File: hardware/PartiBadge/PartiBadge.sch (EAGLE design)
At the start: 18 parts, among them IC1 SI7021-A10-IM, J2 TFT Display Connector

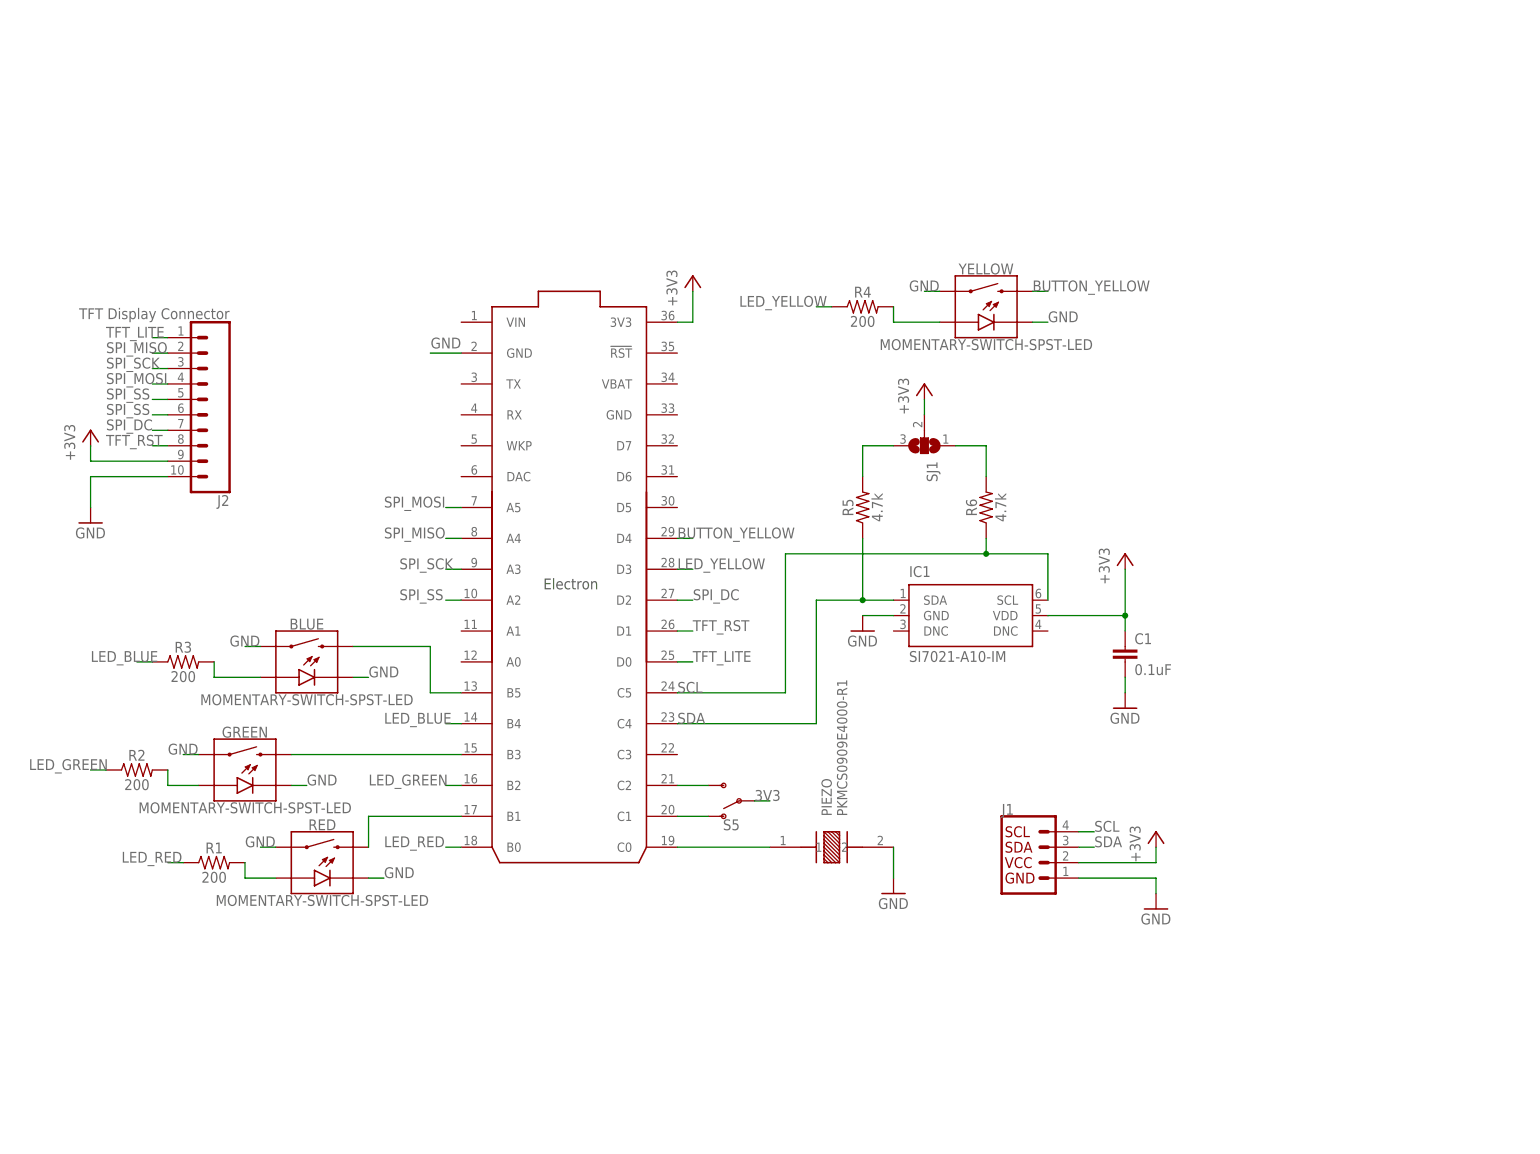
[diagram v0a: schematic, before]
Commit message: tweak layout for smaller badge
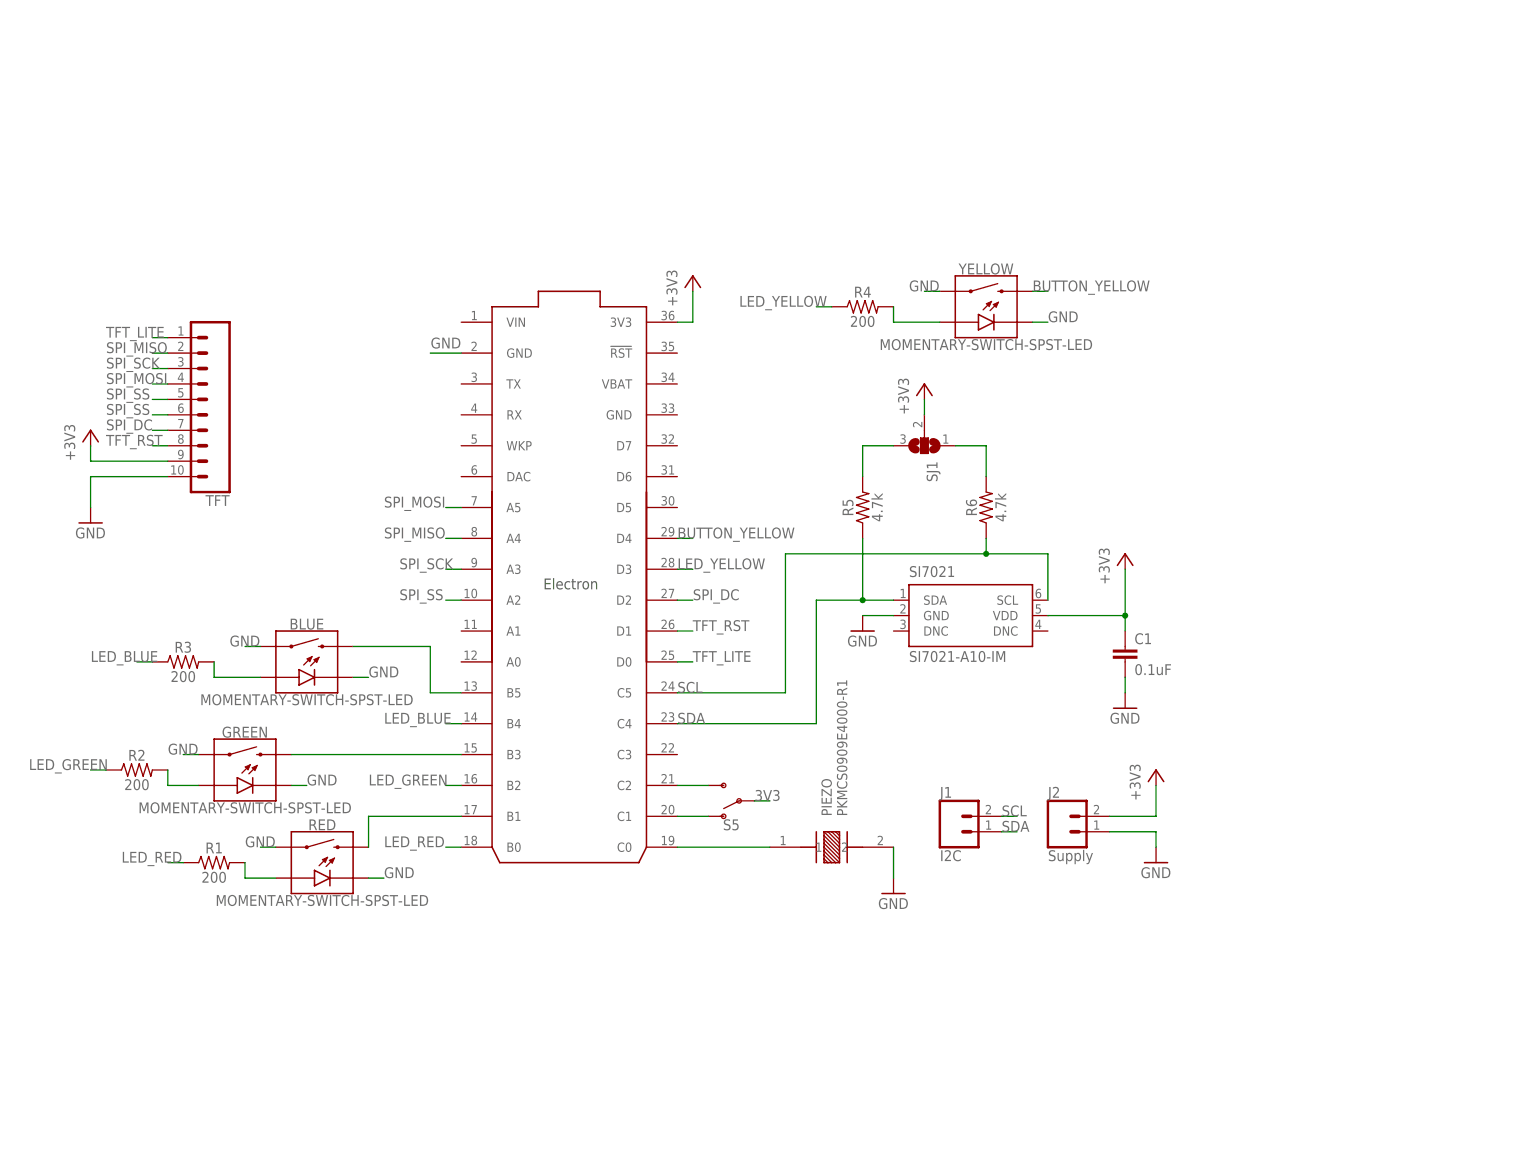
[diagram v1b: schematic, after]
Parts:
- added TFT: (no value), SparkFun-Connectors:CONN_10NO_SILK_PTH_FEMALE
- J1: value (none) -> I2C; device SparkFun-Connectors:I2C_STANDARD -> SparkFun-Connectors:CONN_02
- J2: value TFT Display Connector -> Supply; device SparkFun-Connectors:CONN_10NO_SILK_PTH_FEMALE -> SparkFun-Connectors:CONN_02; SPICEPREFIX X -> (none)
- renumbered IC1 to SI7021, U$1 to ELECTRON
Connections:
- net 3V3: now also J2.2, TFT.9; no longer J1.2, J2.9
- net GND: now also J2.1, TFT.10; no longer J1.1, J2.10
- net SCL: now also J1.2; no longer J1.4
- net SDA: now also J1.1; no longer J1.3
- net SPI_DC: now also TFT.7; no longer J2.7
- net SPI_MISO: now also TFT.2; no longer J2.2
- net SPI_MOSI: now also TFT.4; no longer J2.4
- net SPI_SCK: now also TFT.3; no longer J2.3
- net SPI_SS: now also TFT.5, TFT.6; no longer J2.5, J2.6
- net TFT_LITE: now also TFT.1; no longer J2.1
- net TFT_RST: now also TFT.8; no longer J2.8

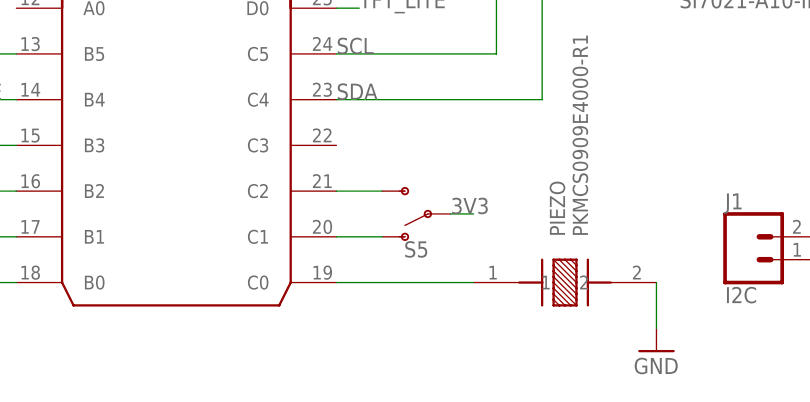
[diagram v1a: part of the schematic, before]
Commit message: increase text and add clr on piezo
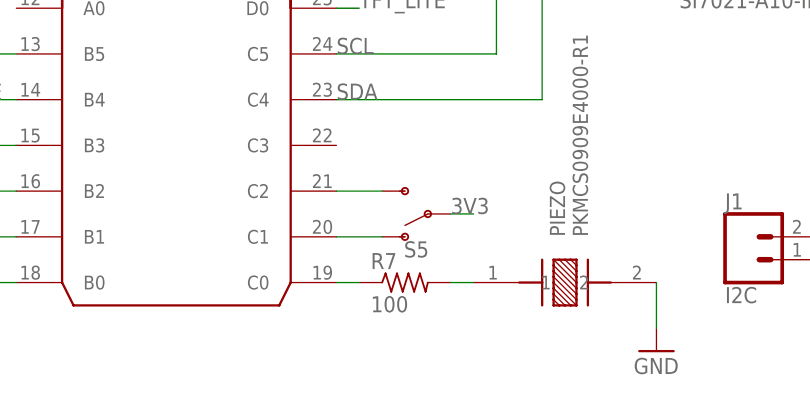
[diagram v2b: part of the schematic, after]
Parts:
- added R7: 100, rcl:R-US_M0805
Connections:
- new net N$13: PIEZO.1, R7.2
- net N$1: now also R7.1; no longer PIEZO.1
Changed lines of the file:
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@@
 <grid distance="0.1" unitdist="inch" unit="inch" style="lines" multiple="1" display="no" altdistance="0.01" altunitdist="inch" altunit="inch"/>
 <layers>
-<layer number="1" name="Top" color="4" fill="1" visible="no" active="no"/>
-<layer number="2" name="Route2" color="1" fill="3" visible="no" active="no"/>
-<layer number="3" name="Route3" color="4" fill="3" visible="no" active="no"/>
-<layer number="4" name="Route4" color="1" fill="4" visible="no" active="no"/>
-<layer number="5" name="Route5" color="4" fill="4" visible="no" active="no"/>
-<layer number="6" name="Route6" color="1" fill="8" visible="no" active="no"/>
-<layer number="7" name="Route7" color="4" fill="8" visible="no" active="no"/>
-<layer number="8" name="Route8" color="1" fill="2" visible="no" active="no"/>
-<layer number="9" name="Route9" color="4" fill="2" visible="no" active="no"/>
-<layer number="10" name="Route10" color="1" fill="7" visible="no" active="no"/>
-<layer number="11" name="Route11" color="4" fill="7" visible="no" active="no"/>
-<layer number="12" name="Route12" color="1" fill="5" visible="no" active="no"/>
-<layer number="13" name="Route13" color="4" fill="5" visible="no" active="no"/>
-<layer number="14" name="Route14" color="1" fill="6" visible="no" active="no"/>
-<layer number="15" name="Route15" color="4" fill="6" visible="no" active="no"/>
-<layer number="16" name="Bottom" color="1" fill="1" visible="no" active="no"/>
-<layer number="17" name="Pads" color="2" fill="1" visible="no" active="no"/>
-<layer number="18" name="Vias" color="2" fill="1" visible="no" active="no"/>
-<layer number="19" name="Unrouted" color="6" fill="1" visible="no" active="no"/>
-<layer number="20" name="Dimension" color="15" fill="1" visible="no" active="no"/>
-<layer number="21" name="tPlace" color="7" fill="1" visible="no" active="no"/>
-<layer number="22" name="bPlace" color="7" fill="1" visible="no" active="no"/>
-<layer number="23" name="tOrigins" color="15" fill="1" visible="no" active="no"/>
-<layer number="24" name="bOrigins" color="15" fill="1" visible="no" active="no"/>
-<layer number="25" name="tNames" color="7" fill="1" visible="no" active="no"/>
-<layer number="26" name="bNames" color="7" fill="1" visible="no" active="no"/>
-<layer number="27" name="tValues" color="7" fill="1" visible="no" active="no"/>
-<layer number="28" name="bValues" color="7" fill="1" visible="no" active="no"/>
+<layer number="1" name="Top" color="4" fill="1" visible="yes" active="no"/>
+<layer number="2" name="Route2" color="1" fill="3" visible="yes" active="no"/>
+<layer number="3" name="Route3" color="4" fill="3" visible="yes" active="no"/>
+<layer number="4" name="Route4" color="1" fill="4" visible="yes" active="no"/>
+<layer number="5" name="Route5" color="4" fill="4" visible="yes" active="no"/>
+<layer number="6" name="Route6" color="1" fill="8" visible="yes" active="no"/>
+<layer number="7" name="Route7" color="4" fill="8" visible="yes" active="no"/>
+<layer number="8" name="Route8" color="1" fill="2" visible="yes" active="no"/>
+<layer number="9" name="Route9" color="4" fill="2" visible="yes" active="no"/>
+<layer number="10" name="Route10" color="1" fill="7" visible="yes" active="no"/>
+<layer number="11" name="Route11" color="4" fill="7" visible="yes" active="no"/>
+<layer number="12" name="Route12" color="1" fill="5" visible="yes" active="no"/>
+<layer number="13" name="Route13" color="4" fill="5" visible="yes" active="no"/>
+<layer number="14" name="Route14" color="1" fill="6" visible="yes" active="no"/>
+<layer number="15" name="Route15" color="4" fill="6" visible="yes" active="no"/>
+<layer number="16" name="Bottom" color="1" fill="1" visible="yes" active="no"/>
+<layer number="17" name="Pads" color="2" fill="1" visible="yes" active="no"/>
+<layer number="18" name="Vias" color="2" fill="1" visible="yes" active="no"/>
+<layer number="19" name="Unrouted" color="6" fill="1" visible="yes" active="no"/>
+<layer number="20" name="Dimension" color="24" fill="1" visible="yes" active="no"/>
+<layer number="21" name="tPlace" color="7" fill="1" visible="yes" active="no"/>
+<layer number="22" name="bPlace" color="7" fill="1" visible="yes" active="no"/>
+<layer number="23" name="tOrigins" color="15" fill="1" visible="yes" active="no"/>
+<layer number="24" name="bOrigins" color="15" fill="1" visible="yes" active="no"/>
+<layer number="25" name="tNames" color="7" fill="1" visible="yes" active="no"/>
+<layer number="26" name="bNames" color="7" fill="1" visible="yes" active="no"/>
+<layer number="27" name="tValues" color="7" fill="1" visible="yes" active="no"/>
+<layer number="28" name="bValues" color="7" fill="1" visible="yes" active="no"/>
 <layer number="29" name="tStop" color="7" fill="3" visible="no" active="no"/>
 <layer number="30" name="bStop" color="7" fill="6" visible="no" active="no"/>
@@
 <layer number="35" name="tGlue" color="7" fill="4" visible="no" active="no"/>
 <layer number="36" name="bGlue" color="7" fill="5" visible="no" active="no"/>
-<layer number="37" name="tTest" color="7" fill="1" visible="no" active="no"/>
-<layer number="38" name="bTest" color="7" fill="1" visible="no" active="no"/>
+<layer number="37" name="tTest" color="7" fill="1" visible="yes" active="no"/>
+<layer number="38" name="bTest" color="7" fill="1" visible="yes" active="no"/>
 <layer number="39" name="tKeepout" color="4" fill="11" visible="no" active="no"/>
 <layer number="40" name="bKeepout" color="1" fill="11" visible="no" active="no"/>
@@
 <layer number="44" name="Drills" color="7" fill="1" visible="no" active="no"/>
 <layer number="45" name="Holes" color="7" fill="1" visible="no" active="no"/>
-<layer number="46" name="Milling" color="3" fill="1" visible="no" active="no"/>
-<layer number="47" name="Measures" color="7" fill="1" visible="no" active="no"/>
-<layer number="48" name="Document" color="7" fill="1" visible="no" active="no"/>
-<layer number="49" name="Reference" color="7" fill="1" visible="no" active="no"/>
-<layer number="50" name="dxf" color="7" fill="1" visible="no" active="no"/>
-<layer number="51" name="tDocu" color="7" fill="1" visible="no" active="no"/>
-<layer number="52" name="bDocu" color="7" fill="1" visible="no" active="no"/>
-<layer number="53" name="tGND_GNDA" color="7" fill="9" visible="no" active="no"/>
-<layer number="54" name="bGND_GNDA" color="1" fill="9" visible="no" active="no"/>
-<layer number="56" name="wert" color="7" fill="1" visible="no" active="no"/>
-<layer number="57" name="tCAD" color="7" fill="1" visible="no" active="no"/>
-<layer number="59" name="tCarbon" color="7" fill="1" visible="no" active="no"/>
-<layer number="60" name="bCarbon" color="7" fill="1" visible="no" active="no"/>
+<layer number="46" name="Milling" color="3" fill="1" visible="yes" active="no"/>
+<layer number="47" name="Measures" color="7" fill="1" visible="yes" active="no"/>
+<layer number="48" name="Document" color="7" fill="1" visible="yes" active="no"/>
+<layer number="49" name="Reference" color="7" fill="1" visible="yes" active="no"/>
+<layer number="50" name="dxf" color="7" fill="1" visible="yes" active="no"/>
+<layer number="51" name="tDocu" color="7" fill="1" visible="yes" active="no"/>
+<layer number="52" name="bDocu" color="7" fill="1" visible="yes" active="no"/>
+<layer number="53" name="tGND_GNDA" color="7" fill="9" visible="yes" active="no"/>
+<layer number="54" name="bGND_GNDA" color="1" fill="9" visible="yes" active="no"/>
+<layer number="56" name="wert" color="7" fill="1" visible="yes" active="no"/>
+<layer number="57" name="tCAD" color="7" fill="1" visible="yes" active="no"/>
+<layer number="59" name="tCarbon" color="7" fill="1" visible="yes" active="no"/>
+<layer number="60" name="bCarbon" color="7" fill="1" visible="yes" active="no"/>
 <layer number="88" name="SimResults" color="9" fill="1" visible="yes" active="yes"/>
 <layer number="89" name="SimProbes" color="9" fill="1" visible="yes" active="yes"/>
@@
 <part name="J1" library="SparkFun-Connectors" library_urn="urn:adsk.eagle:library:513" deviceset="CONN_02" device="" package3d_urn="urn:adsk.eagle:package:38039/1" value="I2C"/>
 <part name="J2" library="SparkFun-Connectors" library_urn="urn:adsk.eagle:library:513" deviceset="CONN_02" device="" package3d_urn="urn:adsk.eagle:package:38039/1" value="Supply"/>
+<part name="R7" library="rcl" library_urn="urn:adsk.eagle:library:334" deviceset="R-US_" device="M0805" package3d_urn="urn:adsk.eagle:package:23556/1" value="100"/>
 </parts>
 <sheets>
@@
 <instance part="J1" gate="G$1" x="93.98" y="10.16"/>
 <instance part="J2" gate="G$1" x="111.76" y="10.16"/>
+<instance part="R7" gate="G$1" x="55.88" y="7.62"/>
 </instances>
 <busses>
 </busses>
 <nets>
-<net name="N$1" class="0">
-<segment>
-<pinref part="ELECTRON" gate="G$1" pin="C0"/>
-<pinref part="PIEZO" gate="G$1" pin="1"/>
-<wire x1="48.26" y1="7.62" x2="63.5" y2="7.62" width="0.1524" layer="91"/>
-</segment>
-</net>
 <net name="GND" class="0">
 <segment>
@@
 <wire x1="-35.56" y1="76.2" x2="-38.1" y2="76.2" width="0.1524" layer="91"/>
 <label x="-45.72" y="76.2" size="1.778" layer="95"/>
+</segment>
+</net>
+<net name="N$1" class="0">
+<segment>
+<pinref part="ELECTRON" gate="G$1" pin="C0"/>
+<pinref part="R7" gate="G$1" pin="1"/>
+<wire x1="48.26" y1="7.62" x2="50.8" y2="7.62" width="0.1524" layer="91"/>
+</segment>
+</net>
+<net name="N$13" class="0">
+<segment>
+<pinref part="R7" gate="G$1" pin="2"/>
+<pinref part="PIEZO" gate="G$1" pin="1"/>
+<wire x1="60.96" y1="7.62" x2="63.5" y2="7.62" width="0.1524" layer="91"/>
 </segment>
 </net>
@@
 packages will not be understood (or retained) with this version.
 </note>
+<note version="8.4" severity="warning">
+Since Version 8.4, EAGLE supports properties for SPICE simulation.
+Probes in schematics and SPICE mapping objects found in parts and library devices
+will not be understood with this version. Update EAGLE to the latest version
+for full support of SPICE simulation.
+</note>
 </compatibility>
